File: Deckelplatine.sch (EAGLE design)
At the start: 59 parts, among them IC1 MAX1487EESA+, IC2 74HCT595D, IC3 74HCT595D, IC4 74HCT595D, IC5 74HCT595D, IC6 74HCT595D, J1 52808-2570, U1 LM2676S, X1 236-406/000-023, X2 233-502

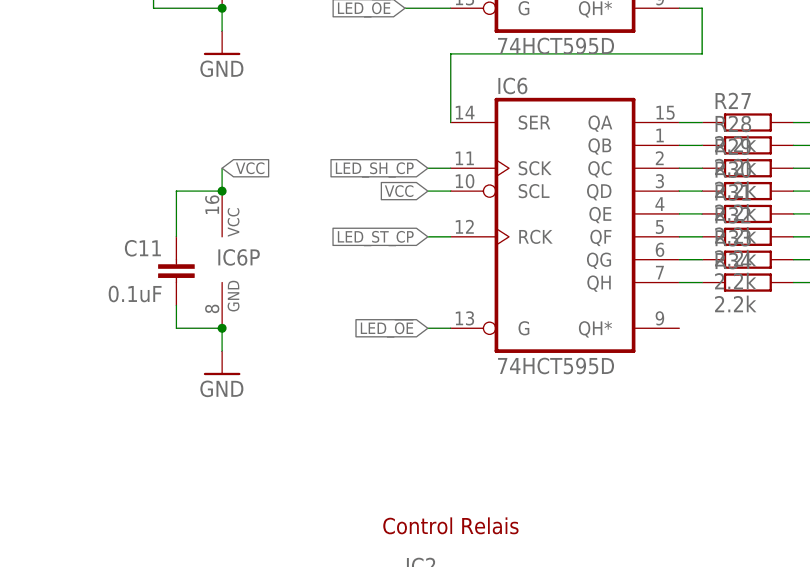
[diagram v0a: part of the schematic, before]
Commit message: Shift Register Pullup Widerstände eingefügt
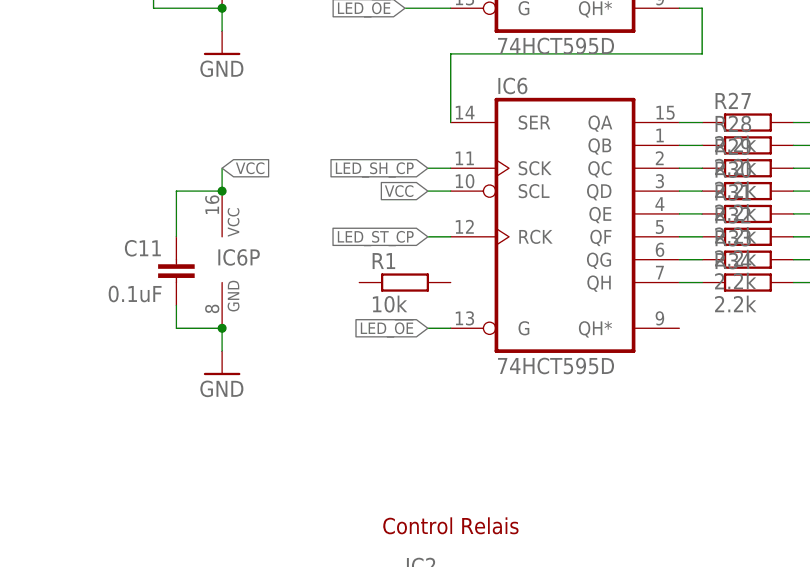
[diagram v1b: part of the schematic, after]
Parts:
- added R1: 10k, RA-GAS Projekte LTD:R-EU_R0603
- IC1: MPN MAX1487EESA+ -> MAX1487EESA+.
- R11, R12, R13, R14, R15, R16, R17, R18, R19, R20, R21, R22, R23, R24, R25, R26, R27, R28, R29, R30, R31, R32, R33, R34: MPN RC0603FR-072K2L -> RC0603FR-072K2L.
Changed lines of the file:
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@@
 <part name="IC1" library="maxim" deviceset="MAX481CSA" device="" value="MAX1487EESA+">
 <attribute name="MF" value="MAXIM INTEGRATED PRODUCTS"/>
-<attribute name="MPN" value="MAX1487EESA+"/>
+<attribute name="MPN" value="MAX1487EESA+."/>
 <attribute name="OC_FARNELL" value="1593310"/>
 <attribute name="PARTNO" value="MAX481CSA"/>
@@
 <part name="R11" library="RA-GAS Projekte LTD" deviceset="R-EU_" device="R0603" value="2.2k">
 <attribute name="MF" value="YAGEO (PHYCOMP)"/>
-<attribute name="MPN" value="RC0603FR-072K2L"/>
+<attribute name="MPN" value="RC0603FR-072K2L."/>
 <attribute name="OC_FARNELL" value="9238522"/>
 <attribute name="PARTNO" value="SMD-0603 2,2K"/>
@@
 <part name="R12" library="RA-GAS Projekte LTD" deviceset="R-EU_" device="R0603" value="2.2k">
 <attribute name="MF" value="YAGEO (PHYCOMP)"/>
-<attribute name="MPN" value="RC0603FR-072K2L"/>
+<attribute name="MPN" value="RC0603FR-072K2L."/>
 <attribute name="OC_FARNELL" value="9238522"/>
 <attribute name="PARTNO" value="SMD-0603 2,2K"/>
@@
 <part name="R13" library="RA-GAS Projekte LTD" deviceset="R-EU_" device="R0603" value="2.2k">
 <attribute name="MF" value="YAGEO (PHYCOMP)"/>
-<attribute name="MPN" value="RC0603FR-072K2L"/>
+<attribute name="MPN" value="RC0603FR-072K2L."/>
 <attribute name="OC_FARNELL" value="9238522"/>
 <attribute name="PARTNO" value="SMD-0603 2,2K"/>
@@
 <part name="R14" library="RA-GAS Projekte LTD" deviceset="R-EU_" device="R0603" value="2.2k">
 <attribute name="MF" value="YAGEO (PHYCOMP)"/>
-<attribute name="MPN" value="RC0603FR-072K2L"/>
+<attribute name="MPN" value="RC0603FR-072K2L."/>
 <attribute name="OC_FARNELL" value="9238522"/>
 <attribute name="PARTNO" value="SMD-0603 2,2K"/>
@@
 <part name="R15" library="RA-GAS Projekte LTD" deviceset="R-EU_" device="R0603" value="2.2k">
 <attribute name="MF" value="YAGEO (PHYCOMP)"/>
-<attribute name="MPN" value="RC0603FR-072K2L"/>
+<attribute name="MPN" value="RC0603FR-072K2L."/>
 <attribute name="OC_FARNELL" value="9238522"/>
 <attribute name="PARTNO" value="SMD-0603 2,2K"/>
@@
 <part name="R16" library="RA-GAS Projekte LTD" deviceset="R-EU_" device="R0603" value="2.2k">
 <attribute name="MF" value="YAGEO (PHYCOMP)"/>
-<attribute name="MPN" value="RC0603FR-072K2L"/>
+<attribute name="MPN" value="RC0603FR-072K2L."/>
 <attribute name="OC_FARNELL" value="9238522"/>
 <attribute name="PARTNO" value="SMD-0603 2,2K"/>
@@
 <part name="R17" library="RA-GAS Projekte LTD" deviceset="R-EU_" device="R0603" value="2.2k">
 <attribute name="MF" value="YAGEO (PHYCOMP)"/>
-<attribute name="MPN" value="RC0603FR-072K2L"/>
+<attribute name="MPN" value="RC0603FR-072K2L."/>
 <attribute name="OC_FARNELL" value="9238522"/>
 <attribute name="PARTNO" value="SMD-0603 2,2K"/>
@@
 <part name="R18" library="RA-GAS Projekte LTD" deviceset="R-EU_" device="R0603" value="2.2k">
 <attribute name="MF" value="YAGEO (PHYCOMP)"/>
-<attribute name="MPN" value="RC0603FR-072K2L"/>
+<attribute name="MPN" value="RC0603FR-072K2L."/>
 <attribute name="OC_FARNELL" value="9238522"/>
 <attribute name="PARTNO" value="SMD-0603 2,2K"/>
@@
 <part name="R19" library="RA-GAS Projekte LTD" deviceset="R-EU_" device="R0603" value="2.2k">
 <attribute name="MF" value="YAGEO (PHYCOMP)"/>
-<attribute name="MPN" value="RC0603FR-072K2L"/>
+<attribute name="MPN" value="RC0603FR-072K2L."/>
 <attribute name="OC_FARNELL" value="9238522"/>
 <attribute name="PARTNO" value="SMD-0603 2,2K"/>
@@
 <part name="R20" library="RA-GAS Projekte LTD" deviceset="R-EU_" device="R0603" value="2.2k">
 <attribute name="MF" value="YAGEO (PHYCOMP)"/>
-<attribute name="MPN" value="RC0603FR-072K2L"/>
+<attribute name="MPN" value="RC0603FR-072K2L."/>
 <attribute name="OC_FARNELL" value="9238522"/>
 <attribute name="PARTNO" value="SMD-0603 2,2K"/>
@@
 <part name="R21" library="RA-GAS Projekte LTD" deviceset="R-EU_" device="R0603" value="2.2k">
 <attribute name="MF" value="YAGEO (PHYCOMP)"/>
-<attribute name="MPN" value="RC0603FR-072K2L"/>
+<attribute name="MPN" value="RC0603FR-072K2L."/>
 <attribute name="OC_FARNELL" value="9238522"/>
 <attribute name="PARTNO" value="SMD-0603 2,2K"/>
@@
 <part name="R22" library="RA-GAS Projekte LTD" deviceset="R-EU_" device="R0603" value="2.2k">
 <attribute name="MF" value="YAGEO (PHYCOMP)"/>
-<attribute name="MPN" value="RC0603FR-072K2L"/>
+<attribute name="MPN" value="RC0603FR-072K2L."/>
 <attribute name="OC_FARNELL" value="9238522"/>
 <attribute name="PARTNO" value="SMD-0603 2,2K"/>
@@
 <part name="R23" library="RA-GAS Projekte LTD" deviceset="R-EU_" device="R0603" value="2.2k">
 <attribute name="MF" value="YAGEO (PHYCOMP)"/>
-<attribute name="MPN" value="RC0603FR-072K2L"/>
+<attribute name="MPN" value="RC0603FR-072K2L."/>
 <attribute name="OC_FARNELL" value="9238522"/>
 <attribute name="PARTNO" value="SMD-0603 2,2K"/>
@@
 <part name="R24" library="RA-GAS Projekte LTD" deviceset="R-EU_" device="R0603" value="2.2k">
 <attribute name="MF" value="YAGEO (PHYCOMP)"/>
-<attribute name="MPN" value="RC0603FR-072K2L"/>
+<attribute name="MPN" value="RC0603FR-072K2L."/>
 <attribute name="OC_FARNELL" value="9238522"/>
 <attribute name="PARTNO" value="SMD-0603 2,2K"/>
@@
 <part name="R25" library="RA-GAS Projekte LTD" deviceset="R-EU_" device="R0603" value="2.2k">
 <attribute name="MF" value="YAGEO (PHYCOMP)"/>
-<attribute name="MPN" value="RC0603FR-072K2L"/>
+<attribute name="MPN" value="RC0603FR-072K2L."/>
 <attribute name="OC_FARNELL" value="9238522"/>
 <attribute name="PARTNO" value="SMD-0603 2,2K"/>
@@
 <part name="R26" library="RA-GAS Projekte LTD" deviceset="R-EU_" device="R0603" value="2.2k">
 <attribute name="MF" value="YAGEO (PHYCOMP)"/>
-<attribute name="MPN" value="RC0603FR-072K2L"/>
+<attribute name="MPN" value="RC0603FR-072K2L."/>
 <attribute name="OC_FARNELL" value="9238522"/>
 <attribute name="PARTNO" value="SMD-0603 2,2K"/>
@@
 <part name="R27" library="RA-GAS Projekte LTD" deviceset="R-EU_" device="R0603" value="2.2k">
 <attribute name="MF" value="YAGEO (PHYCOMP)"/>
-<attribute name="MPN" value="RC0603FR-072K2L"/>
+<attribute name="MPN" value="RC0603FR-072K2L."/>
 <attribute name="OC_FARNELL" value="9238522"/>
 <attribute name="PARTNO" value="SMD-0603 2,2K"/>
@@
 <part name="R28" library="RA-GAS Projekte LTD" deviceset="R-EU_" device="R0603" value="2.2k">
 <attribute name="MF" value="YAGEO (PHYCOMP)"/>
-<attribute name="MPN" value="RC0603FR-072K2L"/>
+<attribute name="MPN" value="RC0603FR-072K2L."/>
 <attribute name="OC_FARNELL" value="9238522"/>
 <attribute name="PARTNO" value="SMD-0603 2,2K"/>
@@
 <part name="R29" library="RA-GAS Projekte LTD" deviceset="R-EU_" device="R0603" value="2.2k">
 <attribute name="MF" value="YAGEO (PHYCOMP)"/>
-<attribute name="MPN" value="RC0603FR-072K2L"/>
+<attribute name="MPN" value="RC0603FR-072K2L."/>
 <attribute name="OC_FARNELL" value="9238522"/>
 <attribute name="PARTNO" value="SMD-0603 2,2K"/>
@@
 <part name="R30" library="RA-GAS Projekte LTD" deviceset="R-EU_" device="R0603" value="2.2k">
 <attribute name="MF" value="YAGEO (PHYCOMP)"/>
-<attribute name="MPN" value="RC0603FR-072K2L"/>
+<attribute name="MPN" value="RC0603FR-072K2L."/>
 <attribute name="OC_FARNELL" value="9238522"/>
 <attribute name="PARTNO" value="SMD-0603 2,2K"/>
@@
 <part name="R31" library="RA-GAS Projekte LTD" deviceset="R-EU_" device="R0603" value="2.2k">
 <attribute name="MF" value="YAGEO (PHYCOMP)"/>
-<attribute name="MPN" value="RC0603FR-072K2L"/>
+<attribute name="MPN" value="RC0603FR-072K2L."/>
 <attribute name="OC_FARNELL" value="9238522"/>
 <attribute name="PARTNO" value="SMD-0603 2,2K"/>
@@
 <part name="R32" library="RA-GAS Projekte LTD" deviceset="R-EU_" device="R0603" value="2.2k">
 <attribute name="MF" value="YAGEO (PHYCOMP)"/>
-<attribute name="MPN" value="RC0603FR-072K2L"/>
+<attribute name="MPN" value="RC0603FR-072K2L."/>
 <attribute name="OC_FARNELL" value="9238522"/>
 <attribute name="PARTNO" value="SMD-0603 2,2K"/>
@@
 <part name="R33" library="RA-GAS Projekte LTD" deviceset="R-EU_" device="R0603" value="2.2k">
 <attribute name="MF" value="YAGEO (PHYCOMP)"/>
-<attribute name="MPN" value="RC0603FR-072K2L"/>
+<attribute name="MPN" value="RC0603FR-072K2L."/>
 <attribute name="OC_FARNELL" value="9238522"/>
 <attribute name="PARTNO" value="SMD-0603 2,2K"/>
@@
 <part name="R34" library="RA-GAS Projekte LTD" deviceset="R-EU_" device="R0603" value="2.2k">
 <attribute name="MF" value="YAGEO (PHYCOMP)"/>
-<attribute name="MPN" value="RC0603FR-072K2L"/>
+<attribute name="MPN" value="RC0603FR-072K2L."/>
 <attribute name="OC_FARNELL" value="9238522"/>
 <attribute name="PARTNO" value="SMD-0603 2,2K"/>
@@
 </part>
 <part name="GND1" library="supply1" deviceset="GND" device=""/>
+<part name="R1" library="RA-GAS Projekte LTD" deviceset="R-EU_" device="R0603" value="10k">
+<attribute name="MF" value="TE CONNECTIVITY / NEOHM"/>
+<attribute name="MPN" value="CPF0603B10KE1"/>
+<attribute name="OC_FARNELL" value="1697388"/>
+</part>
 </parts>
 <sheets>
@@
 <attribute name="VALUE" x="78.74" y="157.48" size="1.778" layer="96"/>
 </instance>
+<instance part="R1" gate="G$1" x="274.32" y="147.32">
+<attribute name="OC_FARNELL" x="274.32" y="147.32" size="1.778" layer="96" display="off"/>
+<attribute name="MF" x="274.32" y="147.32" size="1.27" layer="96" display="off"/>
+<attribute name="MPN" x="274.32" y="147.32" size="1.27" layer="96" display="off"/>
+</instance>
 </instances>

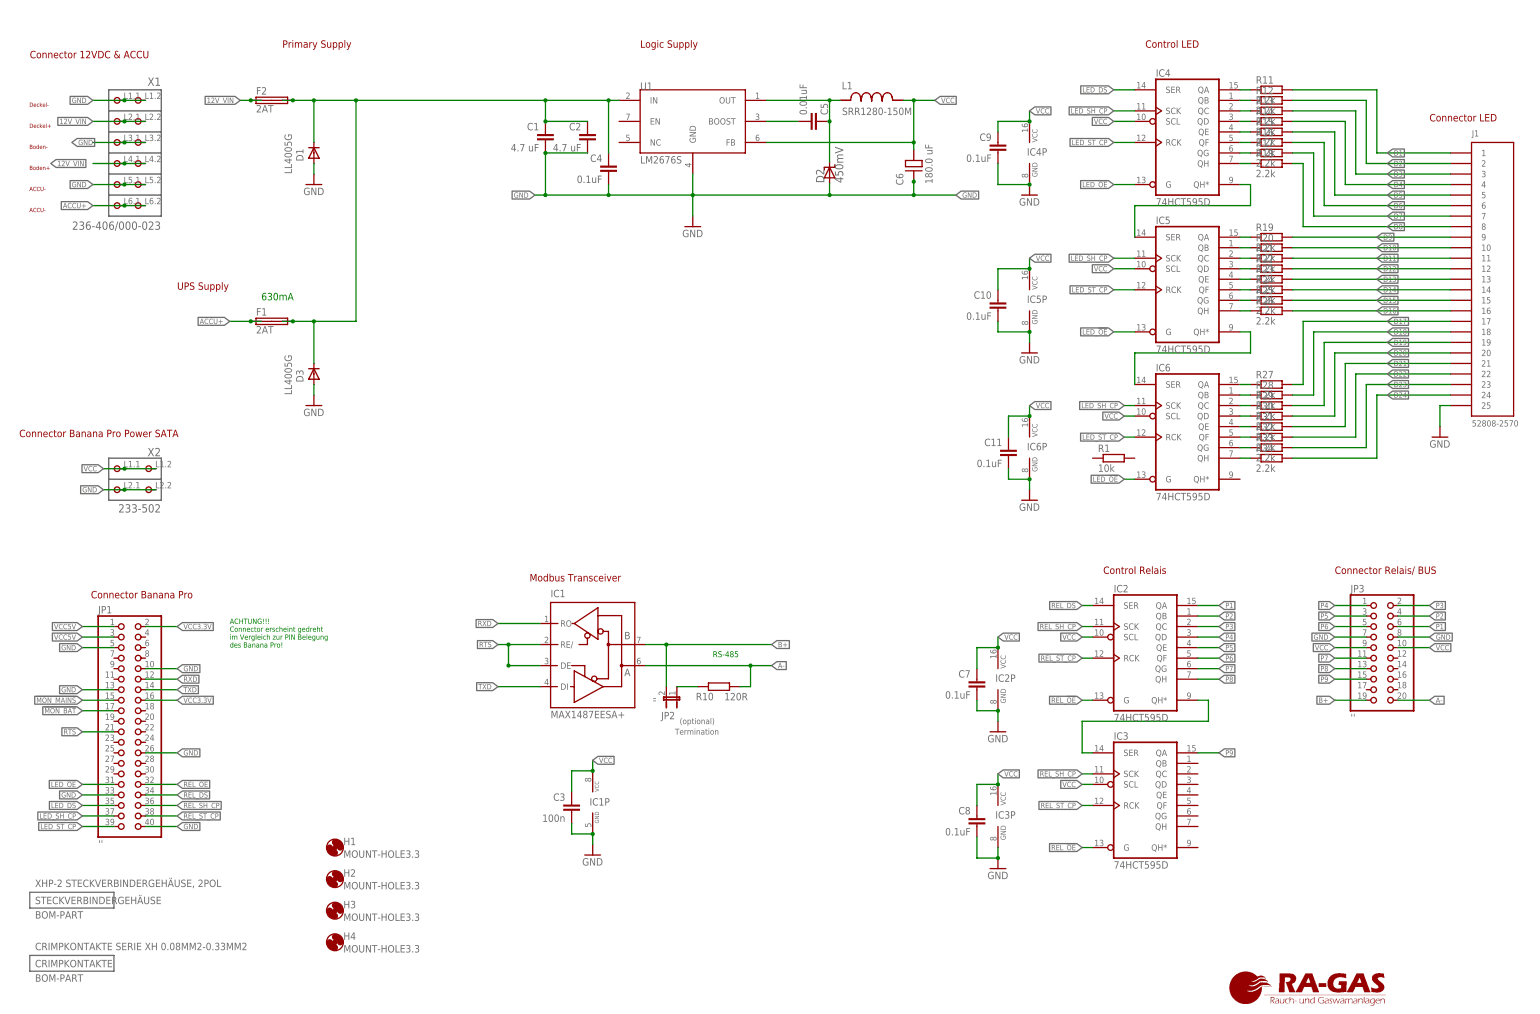
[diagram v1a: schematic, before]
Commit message: Realis Shift Register verschoben
Die Schiebe Register für die Relais waren dem Stecker für die Verbindung zur Bodenplatine im Weg.
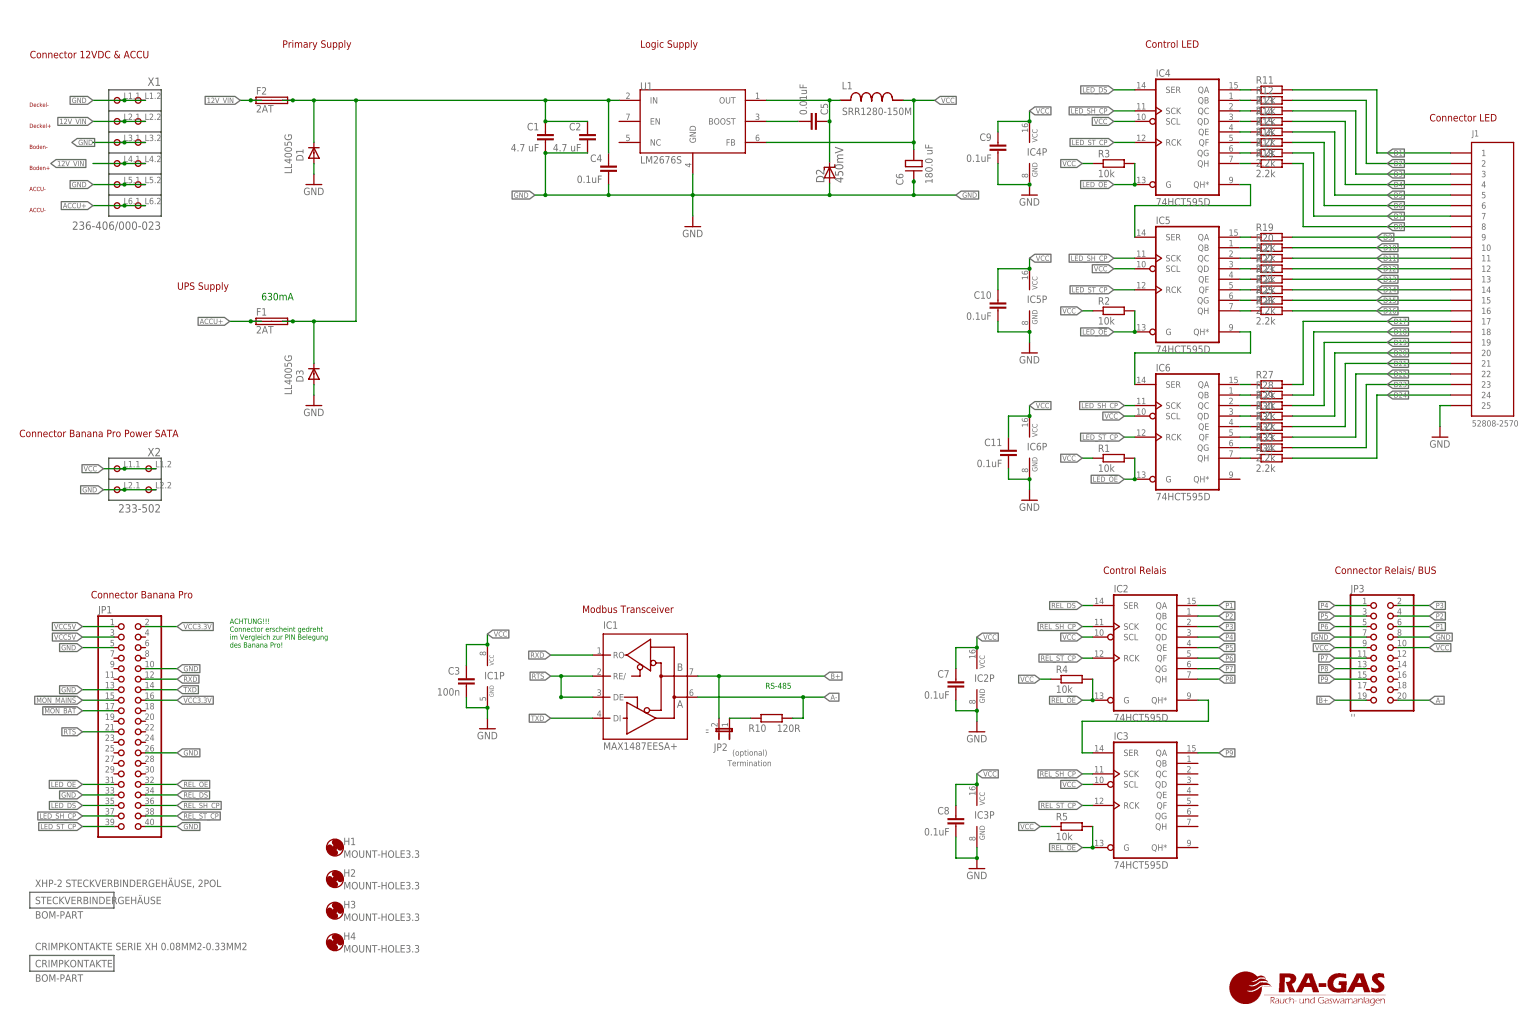
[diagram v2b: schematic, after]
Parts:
- added R2, R3, R4, R5: 10k, RA-GAS Projekte LTD:R-EU_R0603
- JP1: value '' -> (none)
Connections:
- net LED_!OE: now also R1.2, R2.2, R3.2
- net REL_!OE: now also R4.2, R5.2
- net VCC: now also R1.1, R2.1, R3.1, R4.1, R5.1
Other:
- moved on the sheet: C3, C7, C8, IC1, IC1P, IC2P, IC3P, JP2, R10
